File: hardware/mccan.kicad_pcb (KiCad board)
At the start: 4 copper layers, 140 x 100 mm, 237 parts, among them J1 PWR pigtail -> SS1.5 3w, J2 Prog/UART, J3 FL pigtail -> SS1.0 key A / b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, J4 FR pigtail -> SS1.0 key B / g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, J5 RL pigtail -> SS1.0 key C / b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, J6 RR pigtail -> SS1.0 key D / n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, J7 DENALI pigtail -> SS1.5 3w, J8 CAN pigtail -> SS1.0 2w, Q10 IPT008N06NM5LF, Q11 IPT008N06NM5LF, Q12 MMBT3904, Q2 MMBT3904, Q3 MMBT3904, Q4 NX5020UNBKS, Q5 NX5020UNBKS, Q6 NX5020UNBKS, Q7 NX5020UNBKS, Q8 NX5020UNBKS, Q9 NX5020UNBKS, SW1 BOOT, SW2 EN/RESET, U1 LM5164DDA, U10 LTC4380HMS-2, U2 LM5164DDA, U3 LM51571-Q1, U5 ESP32-WROOM-32E-N8, U6 TJA1042T/3, U7 PCA9685PW/Q900, U8 ADG706, U9 BTS7008-2EPA

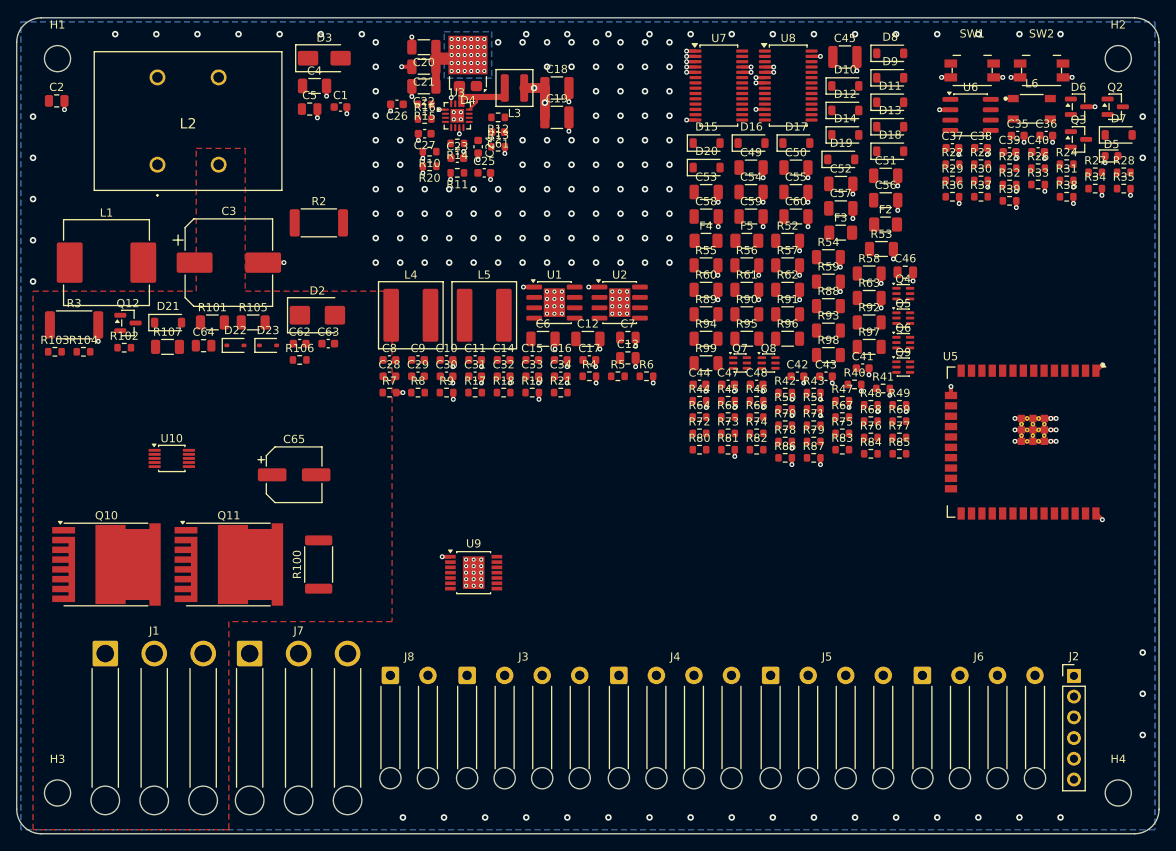
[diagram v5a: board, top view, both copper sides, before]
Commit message: hw(pcb): a grid autorouter for the signal nets
Routes every net that is not GND and not in the FEED, POWER or CAN classes,
with A* over a 0.1 mm two-layer grid: 159 connections, 2321 segments, 255 vias.
Nets are attempted shortest-span first so the tight ones get the channels
before the loose ones fill them, and each net is grown one component at a
time, nearest piece first.

Three geometry rules earn their place, each fixing a class of violation that
passes clearance but fails connection width:

  - A* finishes on whatever cell of the target pad it reached first and then
    wanders inside it, so the segment crossing the pad boundary usually leaves
    through a corner and the overlap is a sliver.  _ar_trim drops the in-pad
    run and _ar_emit replaces it with one lead from the pad centre, which
    crosses the boundary at full track width whatever the angle.

  - ARMap.rect rounds a pad box outward to the nearest grid cell, so the pad's
    copper in the map reaches half a cell past the real edge and A* is
    entitled to finish there.  _ar_pad_at therefore tests against the box
    widened by half a cell; the un-widened test missed exactly the ends
    furthest off centre, which are the ones that need a lead most.

  - A via that half-overlaps a pad -- its own pad; a foreign one is already
    excluded -- joins it through a crescent narrower than either.  The pad
    loop stamps the via halo with net -1 over every pad, so the annulus stays
    off and a track makes the join at full width.

Also fixes pads_board(), which ignored the pad's own rotation within its
footprint: a pad at a non-zero angle in a rotated part landed with the wrong
long axis.

Connection-width violations from the routed board: 139 on the first pass,
0 Pad-to-Track now.  Ten remain, all plane bottlenecks between via antipads,
and 175 unconnected items are still to route.

Co-Authored-By: Claude Opus 5 <noreply@anthropic.com>
Claude-Session: https://claude.ai/code/session_01Bkq7QP4he4cdfxkUNz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
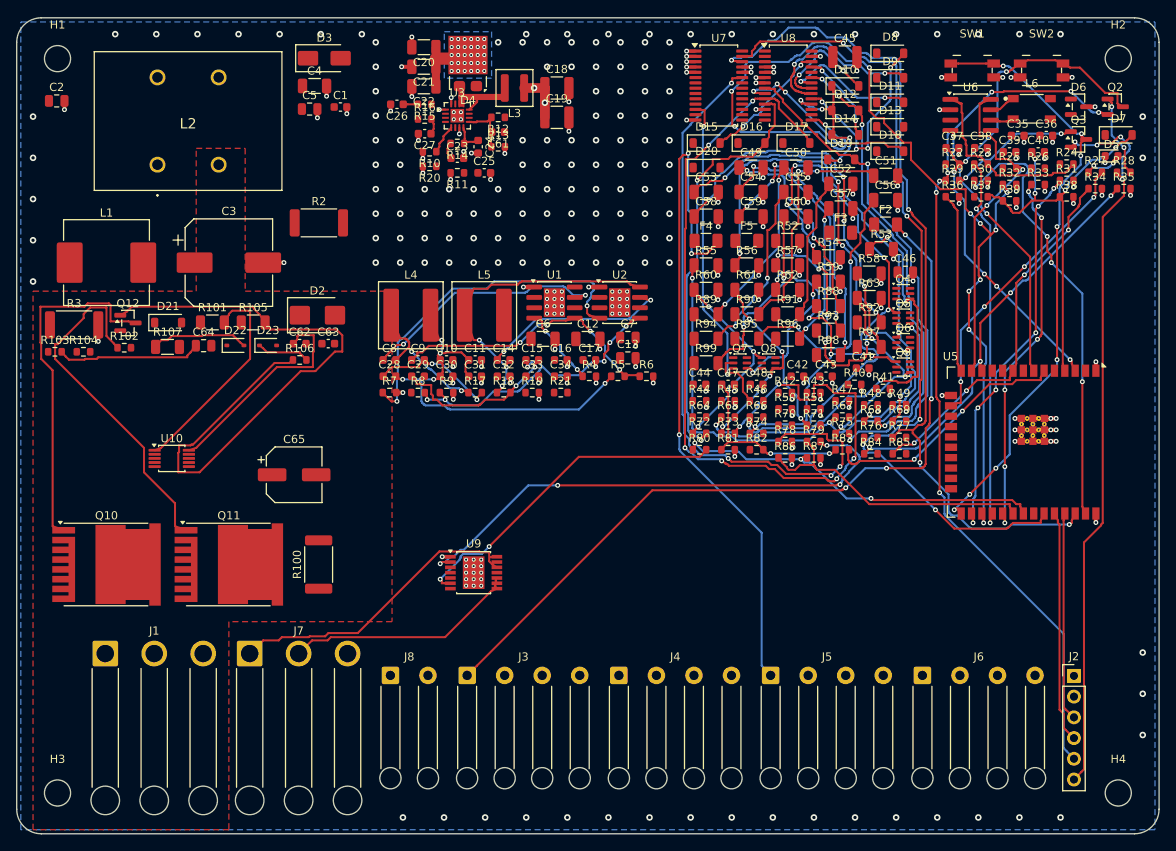
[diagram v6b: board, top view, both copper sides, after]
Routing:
- net /MUX_S2: track 0.00 -> 122.4 mm, vias 0 -> 12
- net /outputs/MUXIN_RR_R: track 0.00 -> 110.2 mm, vias 0 -> 8
- net /mcu_can/DTR: track 0.00 -> 107.4 mm, vias 0 -> 7
- net /I2C_SCL: track 0.00 -> 105.0 mm, vias 0 -> 4
- net /I2C_SDA: track 0.00 -> 102.9 mm, vias 0 -> 5
- net /outputs/+24V_FL: track 0.00 -> 98.3 mm, vias 0 -> 4
- net /mcu_can/RTS: track 0.00 -> 90.5 mm, vias 0 -> 4
- net /outputs/+24V_RL: track 0.00 -> 85.7 mm, vias 0 -> 3
- net Net-(U7-~{OE}): track 0.00 -> 81.7 mm, vias 0 -> 4
- net Net-(Q12-B): track 0.00 -> 79.1 mm
- net /mcu_can/BOOT_N: track 0.00 -> 73.9 mm, vias 0 -> 8
- net /outputs/SENSE_FL_B: track 0.00 -> 69.3 mm, vias 0 -> 6
- net /mcu_can/EN_MCU: track 0.00 -> 66.3 mm, vias 0 -> 6
- net Net-(U9-IN0): track 0.00 -> 64.4 mm, vias 0 -> 4
- net /outputs/SENSE_FR_G: track 0.00 -> 64.0 mm, vias 0 -> 3
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
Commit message: hw(pcb): resolve D4 and U4, give GND_IN its own island, stop leaving stubs
Four things that had all been blocking a clean board, plus the pass of routing
they unblocked.

D4 is a TO-277A, whose third pad is the cathode tab.  Device:D_Schottky has no
pin 3, so schematic parity reported the tab as a net with no corresponding pin
however the pad was aliased -- aliasing pads is not a fix for a symbol that is
missing a pin.  mccan_parts:D_SCHOTTKY_TAB is that symbol with a hidden pin 3
stacked on the cathode, which is what the part actually is.

U4 was BLOCKED since Task 8 step 0 on an apparent pin-1 disagreement between two
figures of DS46371.  There is no disagreement: the Suggested Pad Layout is a bare
land pattern with no pin names, drawn in a different orientation from the Package
Outline, and the three figures that do carry pin names all agree.  Pin 1 top-left
in top view, counter-clockwise; pad 13 is the exposed pad and it is VIN, not GND.
The reasoning is written out in fpmap.py so it is not re-litigated.  fpmap's
unassignable list is now empty and says why it should stay that way.

GND_IN gets its own F.Cu island rather than sharing the pour.  GND and GND_IN are
separate nets that meet at exactly two places, L2 winding B and R3; nothing in DRC
enforces that, because a pour never shorts to a foreign net, so check_grounds.py
is the guard and it now passes: all 12 GND_IN pads inside the island, no GND pads
in it.

_ar_prune was deleting whole tracks when it should have been trimming them, and
was doing its reachability walk without regard for which layer a piece was on.
It is now layer-aware and junction-based, and trims rather than deletes.  That
takes the board from 9 dangling vias and 1 dangling track to none of either.

Also: SolderWire footprints are BOM-excluded in the library and the symbols
disagreed, which parity reported seven times over -- the footprints are right, so
in_bom() now follows them.  Silk references that collided move to F.Fab instead
of bein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
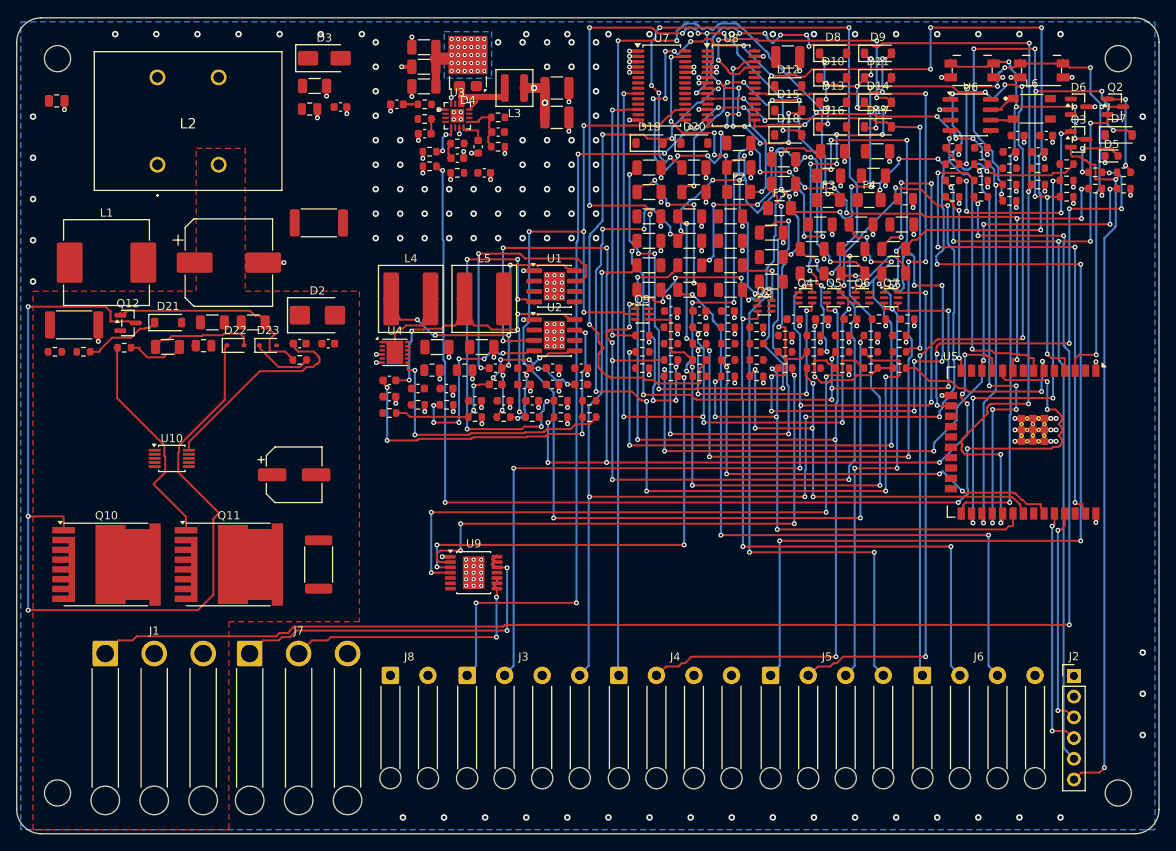
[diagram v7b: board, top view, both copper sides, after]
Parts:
- added U4: DML3017LDC, Package_DFN_QFN:DFN-12-1EP_3x3mm_P0.5mm_EP2.05x2.86mm, F.Cu at (66.3, 61.0)
- moved Q9 32.7 mm to (96.7, 56.3)
- moved R68 29.3 mm to (96.7, 60.9)
- moved R6 28.2 mm to (69.2, 67.4)
- moved R97 27.9 mm to (97.5, 53.3)
- moved R84 26.3 mm to (100.2, 63.9)
- moved R85 26.3 mm to (103.7, 63.9)
- moved C41 24.5 mm to (100.2, 55.9)
- moved C7 24.3 mm to (70.9, 63.2)
- moved R53 23.8 mm to (102.5, 44.3)
- moved D19 23.6 mm to (97.5, 35.4)
- moved C28 23.5 mm to (89.2, 64.9)
- moved R72 23.3 mm to (124.7, 60.9)
- moved R73 23.3 mm to (128.2, 60.9)
- moved R59 22.6 mm to (97.5, 47.3)
- moved F4 20.6 mm to (124.5, 42.3)
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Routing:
- net /IGN_IN: track 0.00 -> 185.0 mm, vias 0 -> 4
- net /outputs/RET_FL_B: track 0.00 -> 159.6 mm, vias 0 -> 8
- net /outputs/PWM_RR_G: track 0.00 -> 146.4 mm, vias 0 -> 7
- net /outputs/RET_FL_R: track 0.00 -> 143.8 mm, vias 0 -> 8
- net /EN_BOOST: track 0.00 -> 140.9 mm, vias 0 -> 6
- net /outputs/+24V_RR: track 0.00 -> 132.3 mm, vias 0 -> 9
- net /EN_3V3SW: track 0.00 -> 128.4 mm, vias 0 -> 10
- net /outputs/+24V_FR: track 0.00 -> 123.8 mm, vias 0 -> 3
- net /outputs/RET_FR_R: track 0.00 -> 118.1 mm, vias 0 -> 5
- net /outputs/SENSE_RL_B: track 24.6 -> 132.5 mm, vias 3 -> 12
- net /I2C_SCL: track 105.0 -> 1.40 mm, vias 4 -> 0
- net Net-(C49-Pad1): track 24.7 -> 127.9 mm, vias 2 -> 14
- net /outputs/PWM_FR_R: track 0.00 -> 97.2 mm, vias 0 -> 7
- net /outputs/RET_RR_R: track 0.00 -> 94.3 mm, vias 0 -> 6
- net /outputs/MUXIN_FL_G: track 21.7 -> 112.5 mm, vias 2 -> 8
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
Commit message: hw(pcb): the external router's copper, frozen in, and the gate that let it through
Task 9's signal bundle now comes from KiCadRoutingTools rather than gen_pcb's own
A*, and the route -> freeze -> emit chain runs end to end for the first time.

KiCad DRC on the result: 0 errors (was 1), 105 unconnected items (was 179),
0 schematic parity issues.  The clearance error at U4 pad 2 is gone, and so are
all 68 silkscreen warnings.  Of the 105 that remain, 53 are on nets this router
was never given -- the power feeds and the CAN pair, which are steps 2 and 3 --
and 52 are its own shortfall over 38 nets.

The run before this one exited 0 and handed back 2177 tracks at 0.0889 mm against
a 0.25 mm request.  --fab-tier is not the flag that stops that; --escalation is,
and its default is documented as going below the board's own minimums.  So:

  check_geometry.py (new) grades copper against the board's OWN declared floors
  and fails the ones under it, a track on a plane layer, and sub-grid junk.  It
  runs first in route_external.py's chain, because a board with copper under its
  floors cannot be frozen however well it grades on connectivity.

  route_external.py now passes --escalation board, --no-bga-zones (there is no
  BGA on this board; the detector reads U7's 0.65 mm TSSOP-28 as a ball grid and
  runs an under-pad rescue at 0.0762 mm), --keep-input-copper, and --json-out.
  The summary confirms them as data: fab_tier_escalations 0, min_delivered
  exactly the board floors.

  freeze_routes.py drops segments under a tenth of the routing grid.  The run
  left two 10 um nubs joining nothing to nothing, too short for the tool's own
  check_weird to see and enough to block the freeze.

  check_vias.py takes a baseline, defaulting to routes_signal.json, so it grades
  gen_pcb's own vias and not the router's deliberate via-in-pad.

Not fab-ready yet, and tracked: 123 router vias at 0.45/0.20 and 73 thermal vias
at 0.50/0.25 both have a 0.125 mm annular ring, under PCBWay's sta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
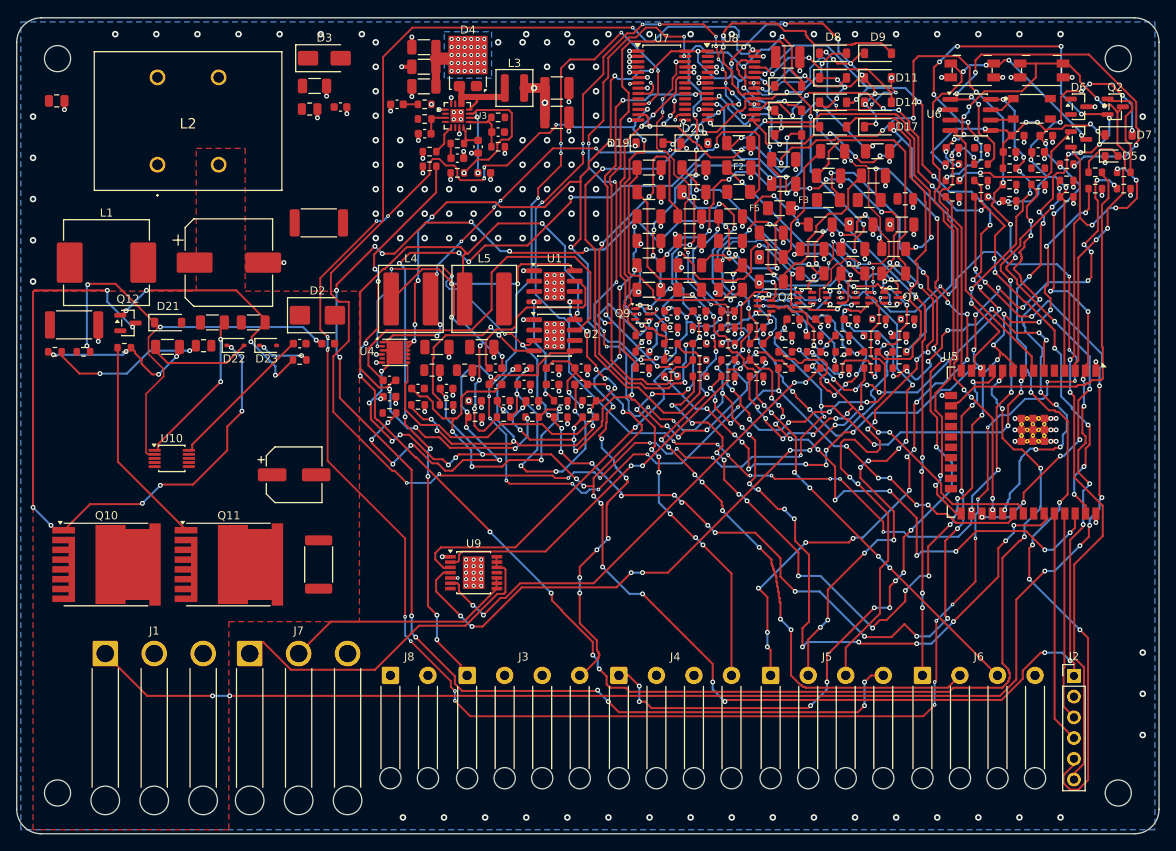
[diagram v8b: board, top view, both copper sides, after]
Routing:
- net /+3V3_ALW: track 19.0 -> 331.2 mm, vias 0 -> 47
- net /outputs/PWM_RL_R: track 33.5 -> 295.9 mm, vias 2 -> 27
- net /+3V3_SW: track 37.4 -> 262.7 mm, vias 11 -> 46
- net /RGB_ISNS: track 1.30 -> 222.0 mm, vias 0 -> 17
- net /outputs/PWM_FR_B: track 1.60 -> 157.3 mm, vias 0 -> 19
- net /outputs/PWM_RR_G: track 146.4 -> 0.59 mm, vias 7 -> 2
- net /MUX_S1: track 54.9 -> 180.3 mm, vias 4 -> 25
- net /outputs/RET_FL_R: track 143.8 -> 23.0 mm, vias 8 -> 6
- net /outputs/RET_FR_R: track 118.1 -> 0.00 mm, vias 5 -> 2
- net /outputs/RET_RL_B: track 67.5 -> 182.4 mm, vias 3 -> 17
- net /outputs/SENSE_RL_B: track 132.5 -> 19.6 mm, vias 12 -> 3
- net /I2C_SCL: track 1.40 -> 111.9 mm, vias 0 -> 19
- net /outputs/RET_FL_B: track 159.6 -> 60.8 mm, vias 8 -> 11
- net /outputs/RET_FR_B: track 1.60 -> 96.8 mm, vias 0 -> 16
- net /outputs/PWM_FR_R: track 97.2 -> 3.07 mm, vias 7 -> 3
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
